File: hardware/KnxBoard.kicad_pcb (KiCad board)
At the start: 2 copper layers, 43 parts, among them J1 SB, J2 KNX, J3 Conn_01x14, J4 Conn_01x02, J5 Conn_01x14, SW1 SW, SW2 SW, U1 STM32L432KCUx, U2 STKNX, X1 SG-3030CM

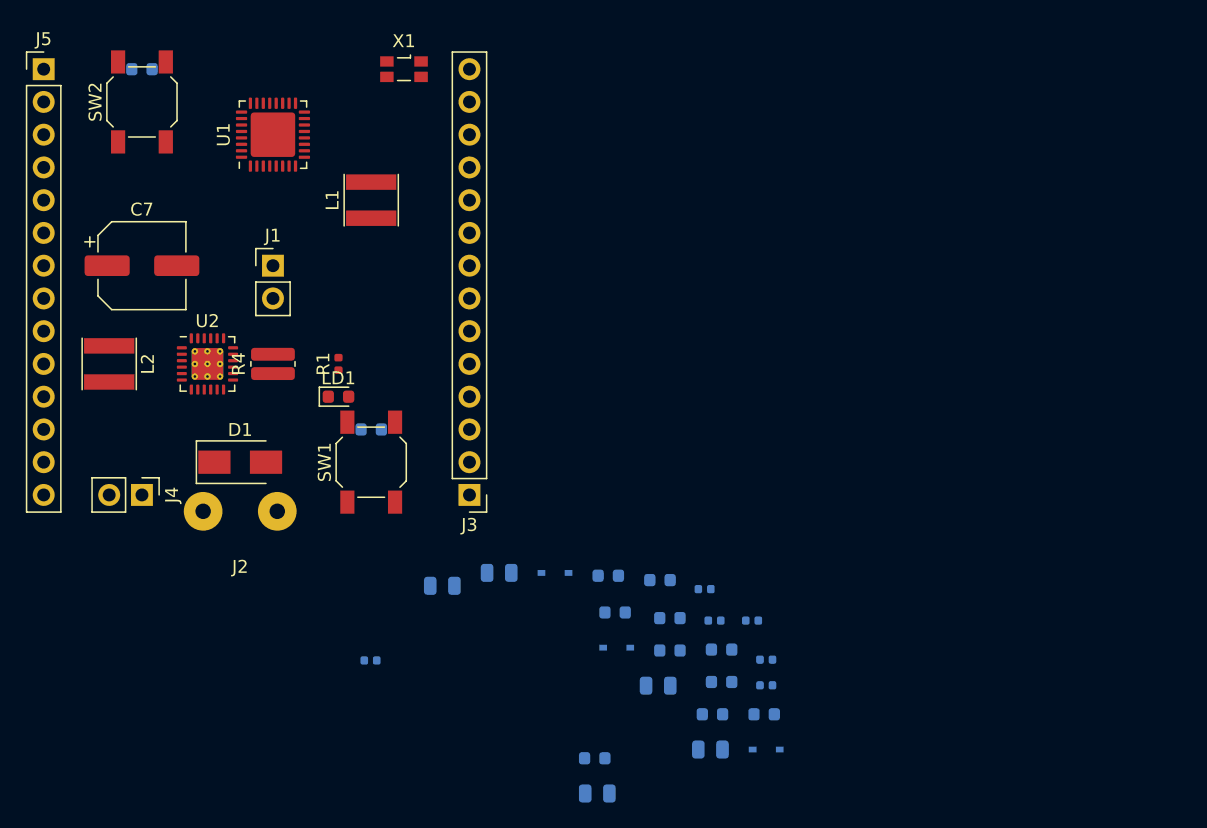
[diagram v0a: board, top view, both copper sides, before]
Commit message: Change architecture, use NCN5130 instead STKNX
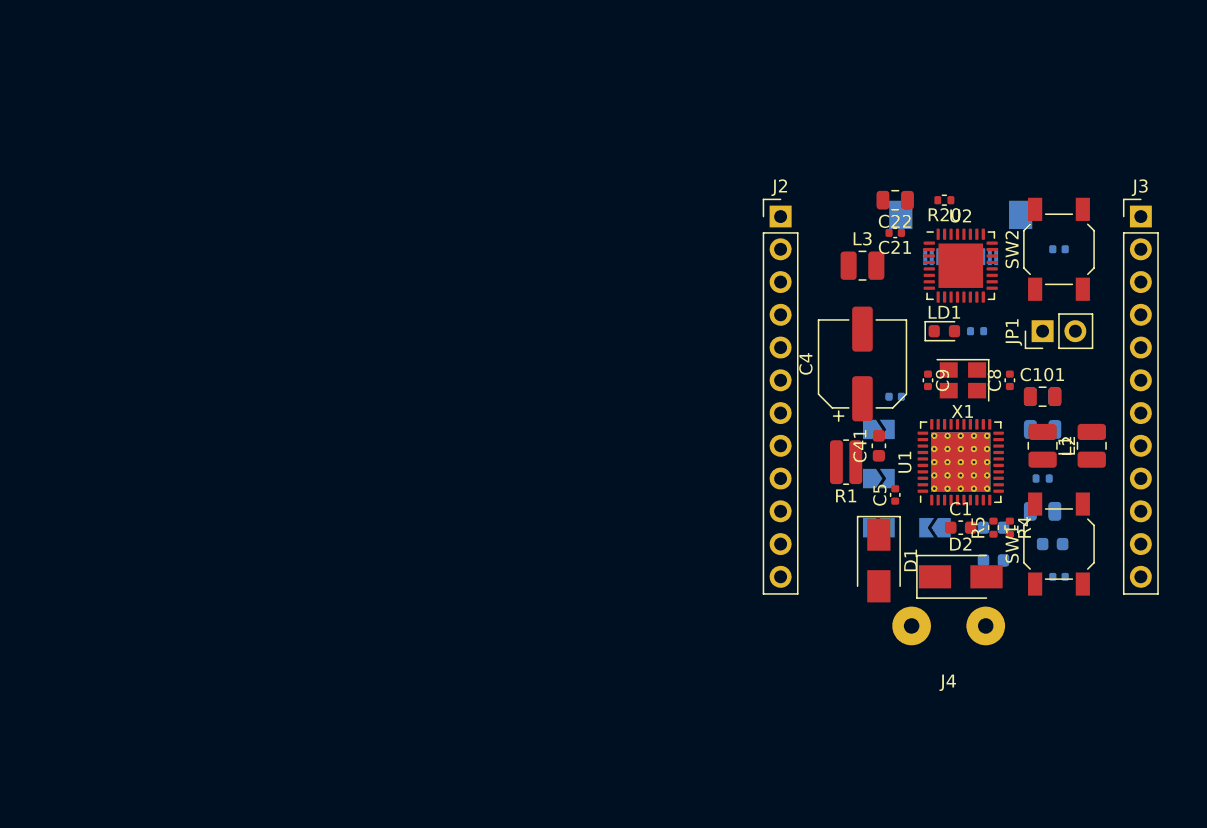
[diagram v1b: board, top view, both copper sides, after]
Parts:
- removed C12, C13: 100nF, Capacitor_SMD:C_0603_1608Metric
- removed C14: 1nF, Capacitor_SMD:C_0603_1608Metric
- removed C15: 100pF, Capacitor_SMD:C_0603_1608Metric
- removed C16, C18: 22uF, Capacitor_SMD:C_0805_2012Metric
- removed C17: 47uF, Capacitor_SMD:C_0805_2012Metric
- removed D3, D4: 1N4148, Diode_SMD:D_SOD-323
- removed J5: Conn_01x14, Connector_PinHeader_2.54mm:PinHeader_1x14_P2.54mm_Vertical
- removed R6: 1K, Resistor_SMD:R_0402_1005Metric
- removed R7: 10K, Resistor_SMD:R_0402_1005Metric
- removed R8: 110K, Resistor_SMD:R_0402_1005Metric
- added C101: 10uF 6.3V ESR < 0.1ohm, Capacitor_SMD:C_0805_2012Metric, F.Cu at (153.7, 104.1)
- added C111: 10uF 6.3V ESR < 0.1ohm, Capacitor_SMD:C_0805_2012Metric, B.Cu at (153.7, 113.0)
- added C20: 100nF 6.3V, Capacitor_SMD:C_0402_1005Metric, B.Cu at (154.9, 92.7)
- added C21: 100nF 6.3V, Capacitor_SMD:C_0402_1005Metric, F.Cu at (142.2, 91.4)
- added C22: 10uF 6.3V ESR < 0.1ohm, Capacitor_SMD:C_0805_2012Metric, F.Cu at (142.2, 88.9)
- added C23: 100nF 6.3V, Capacitor_SMD:C_0402_1005Metric, B.Cu at (154.9, 118.1)
- added C41: 1uF 35V ESR < 2ohm, Capacitor_SMD:C_0603_1608Metric, F.Cu at (141.0, 108.0)
- added JP1: Jumper_2_Open, Connector_PinHeader_2.54mm:PinHeader_1x02_P2.54mm_Vertical, F.Cu at (153.7, 99.1)
- added JP2: SolderJumper_2_Open, Jumper:SolderJumper-2_P1.3mm_Open_TrianglePad1.0x1.5mm, B.Cu at (141.0, 110.5)
- added JP3: SolderJumper_2_Open, Jumper:SolderJumper-2_P1.3mm_Open_TrianglePad1.0x1.5mm, B.Cu at (145.3, 114.3)
- added JP4: SolderJumper_2_Open, Jumper:SolderJumper-2_P1.3mm_Open_TrianglePad1.0x1.5mm, B.Cu at (141.0, 114.3)
- added JP5: SolderJumper_2_Open, Jumper:SolderJumper-2_P1.3mm_Open_TrianglePad1.0x1.5mm, B.Cu at (141.0, 106.7)
- added L3: 220uH, Inductor_SMD:L_1008_2520Metric, F.Cu at (139.7, 94.0)
- added R20: 10K 1/16w, Resistor_SMD:R_0402_1005Metric, F.Cu at (146.1, 88.9)
- added R21: 100R, Resistor_SMD:R_0402_1005Metric, B.Cu at (148.6, 99.1)
- C1: value 100nF -> 47nF 50V; moved to F.Cu
- C10: value 100nF -> 10uF 6.3V ESR < 0.1ohm; footprint Capacitor_SMD:C_0603_1608Metric -> Capacitor_SMD:C_0805_2012Metric
- C11: value 47uF -> 10uF 6.3V ESR < 0.1ohm
- C2: value 100nF -> 220nF 50V
- C3: value 47uF -> 100nF 50V; footprint Capacitor_SMD:C_0805_2012Metric -> Capacitor_SMD:C_0603_1608Metric
- C4: value 100nF -> 100uF 35V; footprint Capacitor_SMD:C_0603_1608Metric -> Capacitor_SMD:CP_Elec_6.3x7.7; moved to F.Cu
- C5: value 470nF -> 100nF 6.3V; footprint Capacitor_SMD:C_0603_1608Metric -> Capacitor_SMD:C_0402_1005Metric; moved to F.Cu
- C6: value 10nF -> 100nF 6.3V; footprint Capacitor_SMD:C_0603_1608Metric -> Capacitor_SMD:C_0402_1005Metric
- C7: value 100uF -> 1uF 35V ESR < 2ohm; footprint Capacitor_SMD:CP_Elec_6.3x7.7 -> Capacitor_SMD:C_0603_1608Metric; moved to B.Cu
- C8, C9: value 47nF -> 10pF 6.3V; footprint Capacitor_SMD:C_0603_1608Metric -> Capacitor_SMD:C_0402_1005Metric; moved to F.Cu
- D1: value SMAJ40CA -> SS16
- D2: value 1N4148 -> 1SMA40CA; footprint Diode_SMD:D_SOD-323 -> Diode_SMD:D_SMA; moved to F.Cu
- J1: value SB -> Conn_01x12_Male; footprint Connector_PinHeader_2.54mm:PinHeader_1x02_P2.54mm_Vertical -> Connector_FFC-FPC:Hirose_FH12-12S-0.5SH_1x12-1MP_P0.50mm_Horizontal; moved to B.Cu
- J2: value KNX -> Conn_01x12; footprint stknx:KNX_Connector -> Connector_PinHeader_2.54mm:PinHeader_1x12_P2.54mm_Vertical
- J3: value Conn_01x14 -> Conn_01x12; footprint Connector_PinHeader_2.54mm:PinHeader_1x14_P2.54mm_Vertical -> Connector_PinHeader_2.54mm:PinHeader_1x12_P2.54mm_Vertical
- J4: value Conn_01x02 -> Conn_01x02_Male; footprint Connector_PinHeader_2.54mm:PinHeader_1x02_P2.54mm_Vertical -> KnxBoard:KNX_Connector
- L1, L2: value 33uH -> 220uH; footprint Inductor_SMD:L_Taiyo-Yuden_NR-40xx -> Inductor_SMD:L_1008_2520Metric
- R1: value 100R -> 27R 1W; footprint Resistor_SMD:R_0402_1005Metric -> Resistor_SMD:R_0612_1632Metric
- R2: value 10K -> 1R 1/16W
- R3: value 4.7M -> 1R 1/16W
- R4: value 68R -> 67.7K 1/16w; footprint Resistor_SMD:R_0612_1632Metric -> Resistor_SMD:R_0402_1005Metric
- R5: value 1K -> 590K 1/16w; moved to F.Cu
- SW1, SW2: value SW -> SW_Push
- U1: value STM32L432KCUx -> NCN5130; footprint Package_DFN_QFN:QFN-32-1EP_5x5mm_P0.5mm_EP3.45x3.45mm -> Package_DFN_QFN:QFN-40-1EP_6x6mm_P0.5mm_EP4.6x4.6mm_ThermalVias
- U2: value STKNX -> STM32L432KCUx; footprint Package_DFN_QFN:VQFN-24-1EP_4x4mm_P0.5mm_EP2.45x2.45mm_ThermalVias -> Package_DFN_QFN:QFN-32-1EP_5x5mm_P0.5mm_EP3.45x3.45mm
- X1: value SG-3030CM -> FA-238; footprint Oscillator:Oscillator_SMD_SeikoEpson_SG3030CM -> Crystal:Crystal_SMD_SeikoEpson_FA238-4Pin_3.2x2.5mm
- moved C2 76.2 mm to (149.9, 116.8)
- moved C7 73.9 mm to (154.4, 115.6)
- moved L2 72.7 mm to (153.7, 108.0)
- moved SW2 72.0 mm to (154.9, 92.7)
- moved J4 64.1 mm to (146.4, 125.7), turned to 0 degrees
- moved U1 59.1 mm to (147.3, 109.2)
- moved L1 59.0 mm to (157.5, 108.0)
- moved U2 58.9 mm to (147.3, 94.0)
- moved R4 58.5 mm to (151.1, 114.3), turned to 270 degrees
- moved J3 56.4 mm to (161.3, 90.2), turned to 0 degrees
- moved R2 54.3 mm to (153.7, 109.2)
- moved SW1 53.7 mm to (154.9, 115.6)
- moved J1 53.4 mm to (147.3, 91.4)
- moved D1 50.1 mm to (141.0, 116.8), turned to 270 degrees
- moved J2 49.7 mm to (133.3, 90.2)
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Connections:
- C1 pad 1: +3V3 -> Net-(C1-Pad1)
- C1 pad 2: /MCU/KNX_PROG_BTN -> Net-(C1-Pad2)
- C10 pad 1: /StKNX/KNX+ -> +3V3
- C10 pad 2: Net-(C10-Pad2) -> GND
- C11 pad 1: Net-(C11-Pad1) -> +12V
- C11 pad 2: Net-(C11-Pad2) -> GND
- C2 pad 1: /MCU/Reset -> Net-(C2-Pad1)
- C2 pad 2: GND -> Net-(C2-Pad2)
- C3 pad 1: +3V3 -> Net-(C3-Pad1)
- C4 pad 1: +3V3 -> Net-(C4-Pad1)
- C5 pad 1: Net-(C5-Pad1) -> GND
- C5 pad 2: GND -> +3V3
- C6 pad 1: Net-(C11-Pad1) -> +3V3
- C6 pad 2: Net-(C6-Pad2) -> GND
- C7 pad 1: /StKNX/VDDHV -> Net-(C7-Pad1)
- C8 pad 1: Net-(C8-Pad1) -> GND
- C8 pad 2: GND -> Net-(C8-Pad2)
- C9 pad 1: /StKNX/VDDHV -> GND
- C9 pad 2: Net-(C8-Pad1) -> Net-(C9-Pad2)
- D1 pad 1: /StKNX/KNX+ -> Net-(C1-Pad2)
- D1 pad 2: GND -> /KNX+
- D2 pad 1: Net-(C11-Pad1) -> /KNX+
- D2 pad 2: /StKNX/KNX+ -> GND
- J1 pad 1: +3V3 -> GND
- J1 pad 2: /StKNX/Vcore -> SWCLK
- J2 pad 1: GND -> Prog
- J2 pad 2: /StKNX/KNX+ -> NRST
- J3 pad 1: GND -> +12V
- J3 pad 10: /MCU/KNX_PROG_BTN -> PB5
- J3 pad 11: /MCU/KNX_PROG_LED -> PB6
- J3 pad 12: /MCU/UART_RX -> PB7
- J3 pad 2: /MCU/PC15 -> GND
- J3 pad 3: /MCU/KNX_TX -> VDD
- J3 pad 4: /MCU/KNX_RX -> PC14
- J3 pad 5: /MCU/KNX_OK -> PC15
- J3 pad 6: /MCU/VCC_OK -> PB0
- J3 pad 7: /MCU/SWCLK -> PB1
- J3 pad 8: /MCU/SWDIO -> Led
- J3 pad 9: /MCU/Reset -> PB4
- J4 pad 1: +12V -> /KNX+
- L1 pad 1: +3V3 -> Net-(L1-Pad1)
- L2 pad 2: +12V -> Net-(L2-Pad2)
- LD1 pad 2: Net-(LD1-Pad2) -> Led
- R1 pad 1: Net-(LD1-Pad2) -> Net-(R1-Pad1)
- R1 pad 2: /MCU/KNX_PROG_LED -> Net-(C1-Pad2)
- R2 pad 1: Net-(R2-Pad1) -> Net-(L1-Pad2)
- R2 pad 2: GND -> +3V3
- R3 pad 1: GND -> Net-(L2-Pad2)
- R3 pad 2: /StKNX/KNX+ -> +12V
- R4 pad 1: Net-(C11-Pad1) -> Net-(JP3-Pad1)
- R4 pad 2: Net-(R4-Pad2) -> +12V
- R5 pad 1: Net-(R5-Pad1) -> GND
- R5 pad 2: Net-(C10-Pad2) -> Net-(JP3-Pad1)
- SW1 pad 1: +3V3 -> VDD
- SW1 pad 2: /MCU/KNX_PROG_BTN -> Prog
- SW2 pad 1: /MCU/Reset -> NRST
- U1 pad 1: +3V3 -> GND
- U1 pad 10: /MCU/PA4 -> Net-(C7-Pad1)
- U1 pad 11: /MCU/PA5 -> Net-(JP3-Pad1)
- U1 pad 12: /MCU/PA6 -> Net-(L2-Pad2)
- U1 pad 13: /MCU/PA7 -> +12V
- U1 pad 14: /MCU/PB0 -> GND
- U1 pad 15: /MCU/PB1 -> Net-(L2-Pad1)
- U1 pad 16: GND -> Net-(C4-Pad1)
- U1 pad 17: +3V3 -> Net-(L1-Pad1)
- U1 pad 18: /MCU/PA8 -> GND
- U1 pad 19: /MCU/KNX_RX -> +3V3
- U1 pad 2: Net-(U1-Pad2) -> GND
- U1 pad 20: /MCU/KNX_OK -> Net-(L1-Pad2)
- U1 pad 21: /MCU/VCC_OK -> Net-(U1-Pad21)
- U1 pad 22: /MCU/KNX_PROG_BTN -> Net-(U1-Pad22)
- U1 pad 23: /MCU/SWDIO -> GND
- U1 pad 24: /MCU/SWCLK -> GND
- U1 pad 25: /MCU/UART_RX -> GND
- U1 pad 26: /MCU/KNX_PROG_LED -> GND
- U1 pad 27: /MCU/PB4 -> RXD
- U1 pad 28: /MCU/PB5 -> TXD
- U1 pad 29: /MCU/PB6 -> GND
- U1 pad 3: /MCU/PC15 -> Net-(R1-Pad1)
- U1 pad 30: /MCU/PB7 -> +3V3
- U1 pad 31: Net-(R2-Pad1) -> GND
- U1 pad 32: GND -> CLK16
- U1 pad 4: /MCU/Reset -> Net-(C1-Pad1)
- U1 pad 5: Net-(L1-Pad2) -> Net-(C3-Pad1)
- U1 pad 6: /MCU/KNX_RX -> Net-(C1-Pad2)
- U1 pad 7: /MCU/KNX_TX -> Net-(C2-Pad1)
- U1 pad 8: /MCU/UART_TX -> Net-(C2-Pad2)
- U1 pad 9: /MCU/PA3 -> Net-(C4-Pad1)
- U2 pad 1: +12V -> VDD
- U2 pad 10: Net-(D4-Pad2) -> PA4
- U2 pad 11: Net-(C11-Pad1) -> PA5
- U2 pad 12: GND -> PA6
- U2 pad 13: Net-(C11-Pad2) -> PA7
- U2 pad 14: /StKNX/VDDHV -> PB0
- U2 pad 15: Net-(L2-Pad1) -> PB1
- U2 pad 17: Net-(C13-Pad2) -> VDD
- U2 pad 18: Net-(C15-Pad1) -> PA8
- U2 pad 19: /MCU/VCC_OK -> RXD
- U2 pad 2: Net-(C6-Pad2) -> PC14
- U2 pad 20: /StKNX/Vcore -> TXD
- U2 pad 21: /MCU/KNX_OK -> PA11
- U2 pad 22: GND -> Prog
- U2 pad 23: /MCU/KNX_RX -> SWDIO
- U2 pad 24: Net-(C14-Pad1) -> SWCLK
- U2 pad 25: GND -> UART_RX
- U2 pad 3: Net-(R4-Pad2) -> PC15
- U2 pad 4: GND -> NRST
- U2 pad 5: Net-(R5-Pad1) -> Net-(L3-Pad2)
- U2 pad 6: Net-(R6-Pad2) -> CLK16
- U2 pad 7: Net-(C8-Pad1) -> PA1
- U2 pad 8: Net-(C5-Pad1) -> UART_TX
- U2 pad 9: /StKNX/VDDHV -> PA3
- X1 pad 1: +3V3 -> Net-(C8-Pad2)
- X1 pad 3: Net-(U1-Pad2) -> Net-(C9-Pad2)
- X1 pad 4: +3V3 -> GND

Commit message: KnxBoard: Continue with layer 2
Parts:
- removed C101, C111: 10uF 6.3V ESR < 0.1ohm, Capacitor_SMD:C_0805_2012Metric
- removed C7: 1uF 35V ESR < 2ohm, Capacitor_SMD:C_0603_1608Metric
- removed JP2, JP3, JP4, JP5: SolderJumper_2_Open, Jumper:SolderJumper-2_P1.3mm_Open_TrianglePad1.0x1.5mm
- added R6: NOTMOUNT, Resistor_SMD:R_0603_1608Metric, F.Cu at (140.2, 111.5)
- C21, C22, C41, C8, C9, D1, D2, L1, L2, R20: moved to B.Cu
- J1: value Conn_01x12_Male -> Conn_01x10; footprint Connector_FFC-FPC:Hirose_FH12-12S-0.5SH_1x12-1MP_P0.50mm_Horizontal -> Connector_PinHeader_1.27mm:PinHeader_2x05_P1.27mm_Vertical; moved to F.Cu
- R21: moved to F.Cu
- moved J3 31.8 mm to (162.6, 121.9), turned to 180 degrees
- moved C4 18.1 mm to (157.2, 106.2)
- moved C41 16.4 mm to (157.2, 106.2)
- moved C11 15.6 mm to (157.2, 121.9), turned to 90 degrees
- moved C8 13.0 mm to (139.2, 108.0), turned to 270 degrees
- moved R21 10.2 mm to (139.7, 104.1), turned to 0 degrees
- moved L3 9.94 mm to (144.1, 102.9), turned to 90 degrees
- moved R20 9.44 mm to (142.9, 97.8)
- moved R1 9.38 mm to (142.9, 117.5)
- moved X1 8.83 mm to (140.3, 108.0), turned to 0 degrees
- moved JP1 8.44 mm to (147.8, 105.2), turned to 180 degrees
- moved C6 8.23 mm to (150.4, 105.4), turned to 90 degrees
- moved J4 7.31 mm to (148.9, 118.9), turned to 180 degrees
- moved LD1 6.84 mm to (139.7, 101.6)
- moved R3 6.18 mm to (159.8, 111.5), turned to 270 degrees
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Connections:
- net Net-(C8-Pad2) renamed /CLK0
- net Net-(C9-Pad2) renamed /CLK1
- C4 pad 1: Net-(C4-Pad1) -> /Vfilt
- C41 pad 1: Net-(C4-Pad1) -> /Vfilt
- J1 pad 1: GND -> Net-(J1-Pad1)
- J1 pad 10: NRST -> VDD
- J1 pad 2: SWCLK -> GND
- J1 pad 3: SWDIO -> NRST
- J1 pad 4: TXD -> UART_RX
- J1 pad 5: RXD -> UART_TX
- J1 pad 6: UART_TX -> SWCLK
- J1 pad 7: UART_RX -> SWDIO
- J1 pad 8: CLK16 -> TXD
- J1 pad 9: RESETB -> RXD
- U1 pad 10: Net-(C7-Pad1) -> /Vfilt
- U1 pad 16: Net-(C4-Pad1) -> /Vfilt
- U1 pad 21: Net-(U1-Pad21) -> +3V3
- U1 pad 36: SAVEB -> PA11
- U1 pad 37: RESETB -> NRST
- U1 pad 41: (no net) -> GND
- U1 pad 9: Net-(C4-Pad1) -> /Vfilt
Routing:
- net GND: track 0.00 -> 99.7 mm, vias 0 -> 7
- net PA8: track 0.00 -> 35.6 mm
- net VDD: track 0.00 -> 34.0 mm, vias 0 -> 3
- net +12V: track 0.00 -> 33.0 mm, vias 0 -> 3
- net PA7: track 0.00 -> 27.6 mm, vias 0 -> 1
- net Net-(C1-Pad2): track 0.00 -> 22.3 mm, vias 0 -> 2
- net /KNX+: track 0.00 -> 15.8 mm
- net /Vfilt: track 0.00 -> 15.1 mm, vias 0 -> 3
- net +3V3: track 0.00 -> 14.2 mm, vias 0 -> 3
- net Net-(L2-Pad2): track 0.00 -> 10.9 mm, vias 0 -> 1
- net Net-(C3-Pad1): track 0.00 -> 9.75 mm, vias 0 -> 1
- net Prog: track 0.00 -> 7.86 mm, vias 0 -> 1
- net Net-(R4-Pad1): track 0.00 -> 7.44 mm
- net /CLK0: track 0.00 -> 6.56 mm, vias 0 -> 1
- net Net-(L1-Pad2): track 0.00 -> 6.40 mm, vias 0 -> 1
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
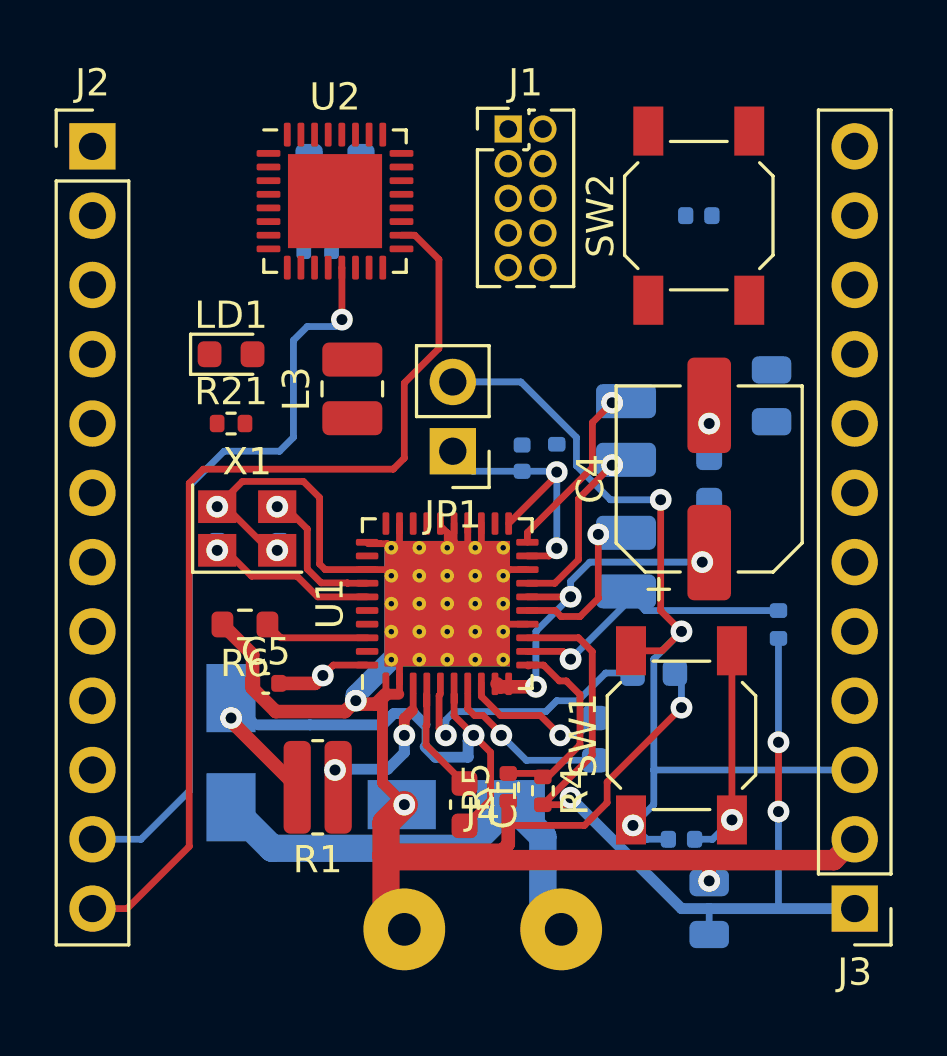
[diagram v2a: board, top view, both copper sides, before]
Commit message: Switch into 4-layers
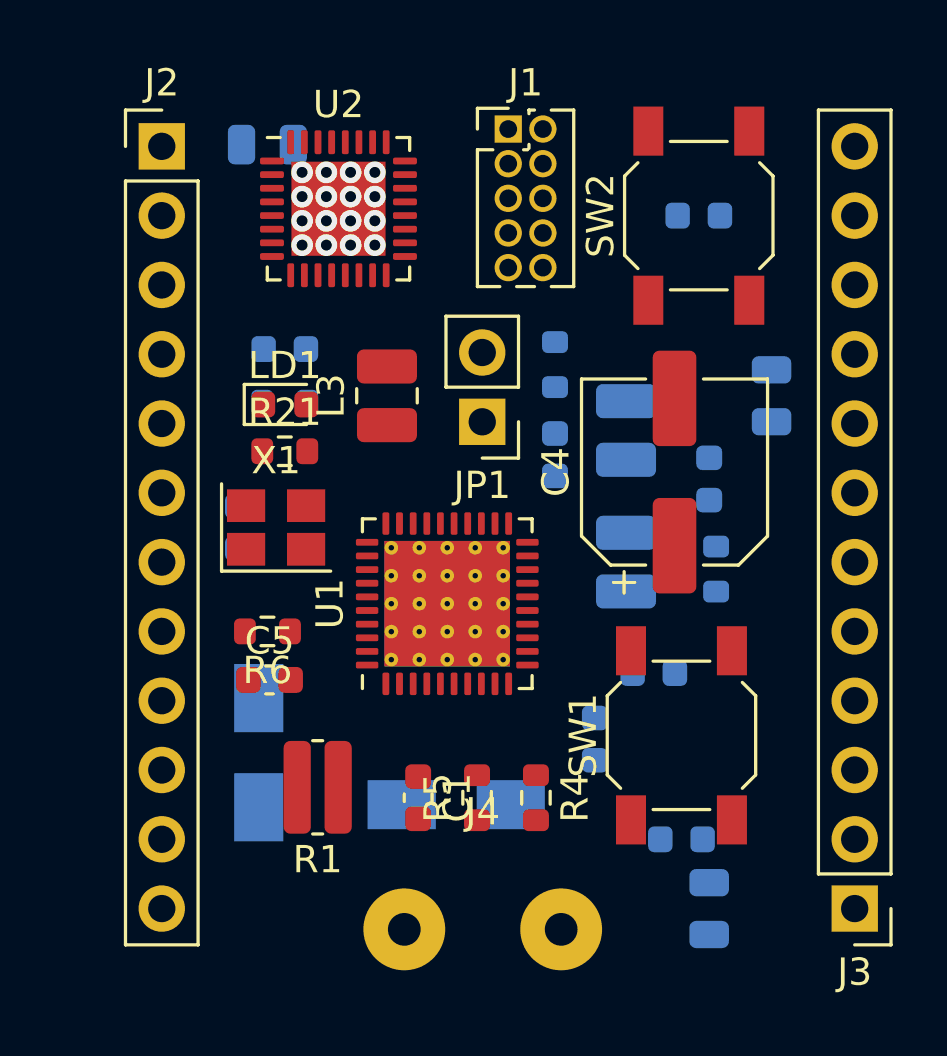
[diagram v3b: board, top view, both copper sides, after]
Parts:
- C20, C21, C23, C5, C6, C8, C9: footprint Capacitor_SMD:C_0402_1005Metric -> Capacitor_SMD:C_0603_1608Metric
- R2, R20, R21, R3: footprint Resistor_SMD:R_0402_1005Metric -> Resistor_SMD:R_0603_1608Metric
- R4: value 67.7K 1/16w -> 56K 1/16w; footprint Resistor_SMD:R_0402_1005Metric -> Resistor_SMD:R_0603_1608Metric
- R5: value 590K 1/16w -> 499K 1/16w; footprint Resistor_SMD:R_0402_1005Metric -> Resistor_SMD:R_0603_1608Metric
- moved R20 5.72 mm to (141.7, 103.4)
- moved C21 5.04 mm to (141.7, 101.4)
- moved R2 3.43 mm to (151.6, 102.0)
- moved R3 3.06 mm to (157.5, 109.5), turned to 90 degrees
- moved LD1 2.70 mm to (141.7, 103.4)
- moved C22 2.57 mm to (141.0, 93.9), turned to 0 degrees
- moved J2 2.54 mm to (137.2, 94.0)
- moved R21 2.22 mm to (141.7, 105.2)
- moved C1 1.72 mm to (146.6, 117.9)
- moved JP1 1.53 mm to (148.9, 104.1)
- moved C4 1.30 mm to (156.0, 105.9)
- moved L3 1.30 mm to (145.4, 103.1)
- moved C6 1.21 mm to (151.6, 105.3)
- moved R5 1.20 mm to (148.7, 117.9)
- moved X1 1.06 mm to (141.4, 108.0)
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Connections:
- J1 pad 1: Net-(J1-Pad1) -> VDD
- J1 pad 10: VDD -> RXD
- J1 pad 3: NRST -> UART_RX
- J1 pad 4: UART_RX -> NRST
- J1 pad 5: UART_TX -> SWCLK
- J1 pad 6: SWCLK -> UART_TX
- J1 pad 8: TXD -> Net-(J1-Pad8)
- J1 pad 9: RXD -> TXD
- J2 pad 1: Prog -> PC14
- J2 pad 10: PA6 -> PA7
- J2 pad 11: PA7 -> PB0
- J2 pad 12: PA8 -> VDD
- J2 pad 2: NRST -> PC15
- J2 pad 3: PA11 -> CLK16
- J2 pad 4: CLK16 -> PA1
- J2 pad 5: PA1 -> UART_TX
- J2 pad 6: UART_TX -> PA3
- J2 pad 7: PA3 -> PA4
- J2 pad 8: PA4 -> PA5
- J2 pad 9: PA5 -> PA6
- J3 pad 10: PB5 -> PB6
- J3 pad 11: PB6 -> PB5
- J3 pad 12: PB7 -> PB4
- J3 pad 3: VDD -> PA11
- J3 pad 4: PC14 -> Prog
- J3 pad 5: PC15 -> Led
- J3 pad 6: PB0 -> PA8
- J3 pad 8: Led -> NRST
- J3 pad 9: PB4 -> PB7
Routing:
- net GND: track 99.7 -> 0.00 mm, vias 7 -> 16
- net PA8: track 35.6 -> 0.00 mm
- net VDD: track 34.0 -> 0.00 mm, vias 3 -> 0
- net +12V: track 33.0 -> 0.00 mm, vias 3 -> 0
- net PA7: track 27.6 -> 0.00 mm, vias 1 -> 0
- net Net-(C1-Pad2): track 22.3 -> 0.00 mm, vias 2 -> 0
- net /KNX+: track 15.8 -> 0.00 mm
- net /Vfilt: track 15.1 -> 0.00 mm, vias 3 -> 0
- net +3V3: track 14.2 -> 0.00 mm, vias 3 -> 0
- net Net-(L2-Pad2): track 10.9 -> 0.00 mm, vias 1 -> 0
- net Net-(C3-Pad1): track 9.75 -> 0.00 mm, vias 1 -> 0
- net Prog: track 7.86 -> 0.00 mm, vias 1 -> 0
- net Net-(R4-Pad1): track 7.44 -> 0.00 mm
- net /CLK0: track 6.56 -> 0.00 mm, vias 1 -> 0
- net Net-(L1-Pad2): track 6.40 -> 0.00 mm, vias 1 -> 0
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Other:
- copper layers 2 -> 4

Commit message: Fin de routage
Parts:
- added R22: 0, Resistor_SMD:R_0603_1608Metric, F.Cu at (141.1, 111.4)
- moved C21 4.71 mm to (145.0, 104.7), turned to 270 degrees
- moved R1 2.01 mm to (142.2, 119.4)
- moved C5 1.52 mm to (141.1, 115.1)
- moved R6 1.52 mm to (141.0, 113.3)
- moved J1 0.65 mm to (150.5, 93.2)
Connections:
- J2 pad 12: VDD -> PA11
- J3 pad 3: PA11 -> VDD
- U1 pad 37: NRST -> Net-(R22-Pad2)
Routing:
- net GND: track 0.00 -> 185.9 mm, vias 16 -> 28
- net Prog: track 0.00 -> 69.4 mm, vias 0 -> 3
- net VDD: track 0.00 -> 66.9 mm, vias 0 -> 4
- net NRST: track 0.00 -> 65.9 mm, vias 0 -> 5
- net Net-(R21-Pad1): track 0.00 -> 52.8 mm, vias 0 -> 2
- net +3V3: track 0.00 -> 49.2 mm, vias 0 -> 4
- net +12V: track 0.00 -> 40.3 mm, vias 0 -> 3
- net PA11: track 0.00 -> 38.0 mm, vias 0 -> 2
- net Led: track 0.00 -> 31.9 mm, vias 0 -> 1
- net PB7: track 0.00 -> 30.4 mm, vias 0 -> 1
- net Net-(R20-Pad1): track 0.00 -> 27.4 mm, vias 0 -> 1
- net PB0: track 0.00 -> 27.2 mm, vias 0 -> 1
- net PB6: track 0.00 -> 26.0 mm, vias 0 -> 1
- net UART_TX: track 0.00 -> 25.9 mm, vias 0 -> 2
- net PB5: track 0.00 -> 25.6 mm, vias 0 -> 1
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- added copper zone on B.Cu, net GND
- added copper zone on In1.Cu, net GND

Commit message: Pad thermique
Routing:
- net GND: track 185.9 -> 200.2 mm
